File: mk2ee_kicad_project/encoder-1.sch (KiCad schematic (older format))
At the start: 15 parts, among them J6 Conn_01x05_Male, J7 Conn_01x05_Male, J8 Conn_01x02_Male, U7 74HC595, U8 AS5047D-ATSM

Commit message: all components are checked
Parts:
- removed J6, J7: Conn_01x05_Male, Connector_Molex:Molex_CLIK-Mate_502443-0570_1x05-1MP_P2.00mm_Vertical, symbol Connector:Conn_01x05_Male
- removed J8: Conn_01x02_Male, Connector_Molex:Molex_CLIK-Mate_502443-0270_1x02-1MP_P2.00mm_Vertical, symbol Connector:Conn_01x02_Male
- added J10: Conn_01x02_Male, MK2Library:Molex_MicroClasp_55932-0210_1x02_P2.00mm_Vertical, symbol Connector:Conn_01x02_Male
- added J8, J9: Conn_02x03_Male, Connector_IDC:IDC-Header_2x03_P2.54mm_Horizontal, symbol Connector:Conn_01x06_Male
- R10, R13: value 45 -> 100; footprint Resistor_SMD:R_0805_2012Metric_Pad1.15x1.40mm_HandSolder -> Resistor_SMD:R_1206_3216Metric; Manufacturer (none) -> MULTICOMP PRO; Name (none) -> MCWR12X1000FTL
- R11, R14: value 86.6 -> 270; footprint Resistor_SMD:R_0805_2012Metric_Pad1.15x1.40mm_HandSolder -> Resistor_SMD:R_1206_3216Metric; Manufacturer (none) -> MULTICOMP PRO; Name (none) -> MCWR12X2700FTL
- R12, R9: value 24 -> 82; footprint Resistor_SMD:R_0805_2012Metric_Pad1.15x1.40mm_HandSolder -> Resistor_SMD:R_1206_3216Metric; Manufacturer (none) -> MULTICOMP PRO; Name (none) -> MCWR12X82R0FTL
- U9: renamed from U7; footprint (none) -> MK2Library:SN74HC595PWR; Manufacturer (none) -> Texas Instruments; Name (none) -> SN74HC595PWR
- renumbered C18 to C20, C19 to C21
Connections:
- net VCC3 is gone; now on net VCCD3v3: C21.1, U8.11 (VDD), U8.12 (VDD3V)
- net CLKEn3: now also J8.3 (Pin_3), J9.3 (Pin_3)
- net GND: now also J10.1 (Pin_1)
- net MISO3: now also J8.4 (Pin_4), J9.4 (Pin_4)
- net PO-CLKEn3: now also J8.1 (Pin_1), J9.1 (Pin_1)
- net SH-CLKEn3: now also J8.5 (Pin_5), J9.5 (Pin_5)
- net SerialDataInEn3: now also J8.2 (Pin_2)
- net SerialDataOutEn3: now also J9.2 (Pin_2)
- net VCCD3v3: now also J10.2 (Pin_2)
- no-connect marks 8 -> 10

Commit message: PCB design is updated
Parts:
- removed C21: 100nF, Capacitor_SMD:CP_Elec_6.3x7.7, symbol Device:CP1
- added C21: 100nF, Capacitor_SMD:C_1206_3216Metric, symbol Device:C
- C20: footprint (none) -> Capacitor_SMD:C_1206_3216Metric; Manufacturer (none) -> Kemet; Name (none) -> C1206C104K5RACTU
- R10, R13: value 100 -> 100R
- R11, R14: value 270 -> 270R
- R12, R9: value 82 -> 82R
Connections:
- net GND: now also C21.2
- net VCCD3v3: now also C21.1
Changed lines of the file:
@@
-$EndComp
-$Comp
-L Device:CP1 C?
-U 1 1 5F504AEC
-P 7400 2600
-AR Path="/5F455032/5F504AEC" Ref="C?"  Part="1"
-AR Path="/5F4C6BF4/5F504AEC" Ref="C?"  Part="1"
-AR Path="/5F4C6CE4/5F504AEC" Ref="C21"  Part="1"
-F 0 "C21" H 7515 2646 50  0000 L CNN
-F 1 "100nF" H 7515 2555 50  0000 L CNN
-F 2 "Capacitor_SMD:CP_Elec_6.3x7.7" H 7400 2600 50  0001 C CNN
-F 3 "~" H 7400 2600 50  0001 C CNN
-F 4 "EDK106M063A9GAA" H 7400 2600 50  0001 C CNN "Name"
-F 5 "Kemet" H 7400 2600 50  0001 C CNN "Manufacturer"
-	1    7400 2600
-	1    0    0    -1
 $EndComp
 $Comp
@@
 AR Path="/5F4C6CE4/5F504B1E" Ref="R11"  Part="1"
 F 0 "R11" H 4580 4304 50  0000 R CNN
-F 1 "270" H 4580 4395 50  0000 R CNN
+F 1 "270R" H 4580 4395 50  0000 R CNN
 F 2 "Resistor_SMD:R_1206_3216Metric" V 4580 4350 50  0001 C CNN
 F 3 "~" H 4650 4350 50  0001 C CNN
@@
 AR Path="/5F4C6CE4/5F504B30" Ref="R10"  Part="1"
 F 0 "R10" H 2080 4404 50  0000 R CNN
-F 1 "100" H 2080 4495 50  0000 R CNN
+F 1 "100R" H 2080 4495 50  0000 R CNN
 F 2 "Resistor_SMD:R_1206_3216Metric" V 2080 4450 50  0001 C CNN
 F 3 "~" H 2150 4450 50  0001 C CNN
@@
 AR Path="/5F4C6CE4/5F504B49" Ref="R9"  Part="1"
 F 0 "R9" H 1680 4304 50  0000 R CNN
-F 1 "82" H 1680 4395 50  0000 R CNN
+F 1 "82R" H 1680 4395 50  0000 R CNN
 F 2 "Resistor_SMD:R_1206_3216Metric" V 1680 4350 50  0001 C CNN
 F 3 "~" H 1750 4350 50  0001 C CNN
@@
 Wire Wire Line
 	2750 2200 2750 1300
-Connection ~ 2750 1300
 Wire Wire Line
 	2750 1300 3300 1300
-Wire Wire Line
-	2250 1300 2450 1300
-$Comp
-L Device:C C20
-U 1 1 5F941CAA
-P 2450 1450
-F 0 "C20" H 2565 1496 50  0000 L CNN
-F 1 "100nF" H 2565 1405 50  0000 L CNN
-F 2 "" H 2488 1300 50  0001 C CNN
-F 3 "~" H 2450 1450 50  0001 C CNN
-	1    2450 1450
-	1    0    0    -1
-$EndComp
-Connection ~ 2450 1300
-Wire Wire Line
-	2450 1300 2750 1300
 $Comp
 L power:GND #PWR0148
@@
 AR Path="/5F4C6CE4/6022AF4A" Ref="R12"  Part="1"
 F 0 "R12" H 1680 5604 50  0000 R CNN
-F 1 "82" H 1680 5695 50  0000 R CNN
+F 1 "82R" H 1680 5695 50  0000 R CNN
 F 2 "Resistor_SMD:R_1206_3216Metric" V 1680 5650 50  0001 C CNN
 F 3 "~" H 1750 5650 50  0001 C CNN
@@
 AR Path="/5F4C6CE4/6022B39A" Ref="R13"  Part="1"
 F 0 "R13" H 2080 5704 50  0000 R CNN
-F 1 "100" H 2080 5795 50  0000 R CNN
+F 1 "100R" H 2080 5795 50  0000 R CNN
 F 2 "Resistor_SMD:R_1206_3216Metric" V 2080 5750 50  0001 C CNN
 F 3 "~" H 2150 5750 50  0001 C CNN
@@
 AR Path="/5F4C6CE4/6022C64F" Ref="R14"  Part="1"
 F 0 "R14" H 4580 5604 50  0000 R CNN
-F 1 "270" H 4580 5695 50  0000 R CNN
+F 1 "270R" H 4580 5695 50  0000 R CNN
 F 2 "Resistor_SMD:R_1206_3216Metric" V 4580 5650 50  0001 C CNN
 F 3 "~" H 4650 5650 50  0001 C CNN
@@
 Text Label 3150 1300 2    50   ~ 0
 pwr11
+$Comp
+L Device:C C21
+U 1 1 6032EA5A
+P 7400 2600
+AR Path="/5F4C6CE4/6032EA5A" Ref="C21"  Part="1"
+AR Path="/5F475AB3/6032EA5A" Ref="C?"  Part="1"
+F 0 "C21" H 7515 2646 50  0000 L CNN
+F 1 "100nF" H 7515 2555 50  0000 L CNN
+F 2 "Capacitor_SMD:C_1206_3216Metric" H 7438 2450 50  0001 C CNN
+F 3 "~" H 7400 2600 50  0001 C CNN
+F 4 "C1206C104K5RACTU" H 7400 2600 50  0001 C CNN "Name"
+F 5 "Kemet" H 7400 2600 50  0001 C CNN "Manufacturer"
+	1    7400 2600
+	1    0    0    -1
+$EndComp
+$Comp
+L Device:C C20
+U 1 1 603306B0
+P 2450 1450
+AR Path="/5F4C6CE4/603306B0" Ref="C20"  Part="1"
+AR Path="/5F475AB3/603306B0" Ref="C?"  Part="1"
+F 0 "C20" H 2565 1496 50  0000 L CNN
+F 1 "100nF" H 2565 1405 50  0000 L CNN
+F 2 "Capacitor_SMD:C_1206_3216Metric" H 2488 1300 50  0001 C CNN
+F 3 "~" H 2450 1450 50  0001 C CNN
+F 4 "C1206C104K5RACTU" H 2450 1450 50  0001 C CNN "Name"
+F 5 "Kemet" H 2450 1450 50  0001 C CNN "Manufacturer"
+	1    2450 1450
+	1    0    0    -1
+$EndComp
+Wire Wire Line
+	2250 1300 2450 1300
+Connection ~ 2750 1300
+Connection ~ 2450 1300
+Wire Wire Line
+	2450 1300 2750 1300
 $EndSCHEMATC

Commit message: all components are connected
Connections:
- net CLKEn3: now also J8.4 (Pin_4), J9.4 (Pin_4); no longer J8.3 (Pin_3), J9.3 (Pin_3)
- net CSn3: now also U9.7 (QH); no longer U9.15 (QA)
- net LED2-B3: now also U9.4 (QE); no longer U9.6 (QG)
- net LED2-R3: now also U9.6 (QG); no longer U9.4 (QE)
- net MISO3: now also J8.6 (Pin_6), J9.2 (Pin_2); no longer J8.4 (Pin_4), J9.4 (Pin_4)
- net PO-CLKEn3: now also J8.3 (Pin_3), J9.3 (Pin_3); no longer J8.1 (Pin_1), J9.1 (Pin_1)
- net SH-CLKEn3: now also J9.1 (Pin_1); no longer J9.5 (Pin_5)
- net SerialDataInEn3: now also J8.1 (Pin_1); no longer J8.2 (Pin_2)
- net SerialDataOutEn3: now also J9.5 (Pin_5); no longer J9.2 (Pin_2)
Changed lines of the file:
@@
 Comment4 ""
 $EndDescr
-Text GLabel 3950 1900 2    50   Output ~ 0
+Text GLabel 3950 2600 2    50   Output ~ 0
 CSn3
 Text GLabel 3950 2000 2    50   Output ~ 0
@@
 Text GLabel 3950 2200 2    50   Output ~ 0
 LED1-B3
-Text GLabel 3950 2300 2    50   Output ~ 0
+Text GLabel 3950 2500 2    50   Output ~ 0
 LED2-R3
 Text GLabel 3950 2400 2    50   Output ~ 0
 LED2-G3
-NoConn ~ 3700 2600
-Wire Wire Line
-	3700 1900 3950 1900
+Wire Wire Line
+	3700 2600 3950 2600
 Wire Wire Line
 	3700 2000 3950 2000
@@
 	3700 2200 3950 2200
 Wire Wire Line
-	3700 2300 3950 2300
+	3700 2500 3950 2500
 Wire Wire Line
 	3700 2400 3950 2400
-Text GLabel 9150 2000 0    50   Output ~ 0
+Text GLabel 9150 1900 0    50   Output ~ 0
 CLKEn3
-Text GLabel 9150 1900 0    50   Input ~ 0
+Text GLabel 9150 1700 0    50   Input ~ 0
 MISO3
 Text GLabel 9150 1800 0    50   Output ~ 0
 SH-CLKEn3
-Text GLabel 9150 2100 0    50   Output ~ 0
+Text GLabel 9150 2200 0    50   Output ~ 0
 SerialDataInEn3
-Text GLabel 9150 2200 0    50   Output ~ 0
+Text GLabel 9150 2000 0    50   Output ~ 0
 PO-CLKEn3
 Wire Wire Line
 	9150 1800 9400 1800
 Wire Wire Line
+	9150 1700 9400 1700
+Wire Wire Line
 	9150 1900 9400 1900
 Wire Wire Line
+	9150 2200 9400 2200
+Wire Wire Line
 	9150 2000 9400 2000
 Wire Wire Line
-	9150 2100 9400 2100
-Wire Wire Line
-	9150 2200 9400 2200
+	9150 3050 9400 3050
+Wire Wire Line
+	9150 2950 9400 2950
+Wire Wire Line
+	9150 2750 9400 2750
 Wire Wire Line
 	9150 2650 9400 2650
 Wire Wire Line
-	9150 2750 9400 2750
-Wire Wire Line
 	9150 2850 9400 2850
-Wire Wire Line
-	9150 2950 9400 2950
-Wire Wire Line
-	9150 3050 9400 3050
 Text GLabel 2250 1300 0    50   Input ~ 0
 VCCD3v3
@@
 Wire Wire Line
 	2650 1900 2900 1900
-Text GLabel 3950 2500 2    50   Output ~ 0
+Text GLabel 3950 2300 2    50   Output ~ 0
 LED2-B3
 Wire Wire Line
-	3700 2500 3950 2500
+	3700 2300 3950 2300
+Text GLabel 9150 2750 0    50   Input ~ 0
+CLKEn3
+Text GLabel 9150 2950 0    50   Output ~ 0
+MISO3
+Text GLabel 9150 3050 0    50   Input ~ 0
+SH-CLKEn3
+Text GLabel 9150 2650 0    50   Input ~ 0
+SerialDataOutEn3
 Text GLabel 9150 2850 0    50   Input ~ 0
-CLKEn3
-Text GLabel 9150 2750 0    50   Output ~ 0
-MISO3
-Text GLabel 9150 2650 0    50   Input ~ 0
-SH-CLKEn3
-Text GLabel 9150 2950 0    50   Input ~ 0
-SerialDataOutEn3
-Text GLabel 9150 3050 0    50   Input ~ 0
 PO-CLKEn3
 $Comp
@@
 	-1   0    0    1
 $EndComp
-NoConn ~ 9400 2550
-NoConn ~ 9400 1700
 $Comp
 L Connector:Conn_01x02_Male J?
@@
 Wire Wire Line
 	2450 1300 2750 1300
+NoConn ~ 3700 1900
+NoConn ~ 9400 2100
+NoConn ~ 9400 2550
 $EndSCHEMATC

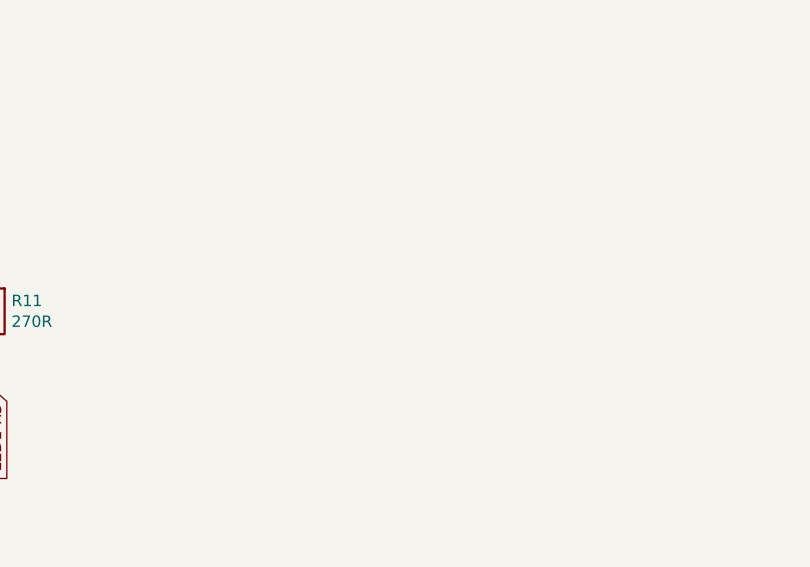
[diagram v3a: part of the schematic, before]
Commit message: New 3D model of Base part and PCB design is fixed
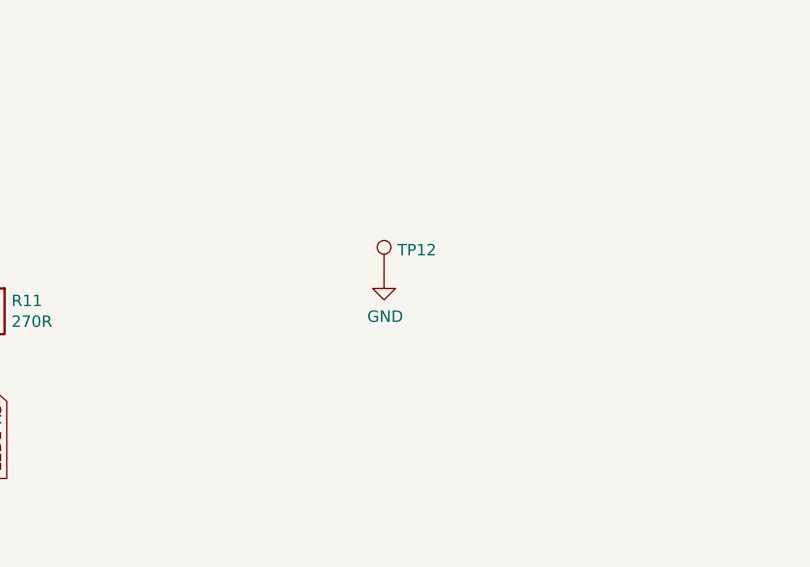
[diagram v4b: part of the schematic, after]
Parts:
- added TP12: TestPoint, TestPoint:TestPoint_THTPad_D1.0mm_Drill0.5mm, symbol Connector:TestPoint
- C20, C21: footprint Capacitor_SMD:C_1206_3216Metric -> Capacitor_SMD:C_1206_3216Metric_Pad1.42x1.75mm_HandSolder
- R10, R11, R12, R13, R14, R9: footprint Resistor_SMD:R_1206_3216Metric -> Resistor_SMD:R_1206_3216Metric_Pad1.42x1.75mm_HandSolder
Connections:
- net GND: now also TP12.1
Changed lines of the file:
@@
 F 0 "R11" H 4580 4304 50  0000 R CNN
 F 1 "270R" H 4580 4395 50  0000 R CNN
-F 2 "Resistor_SMD:R_1206_3216Metric" V 4580 4350 50  0001 C CNN
+F 2 "Resistor_SMD:R_1206_3216Metric_Pad1.42x1.75mm_HandSolder" V 4580 4350 50  0001 C CNN
 F 3 "~" H 4650 4350 50  0001 C CNN
 F 4 "MCWR12X2700FTL" H 4650 4350 50  0001 C CNN "Name"
@@
 F 0 "R10" H 2080 4404 50  0000 R CNN
 F 1 "100R" H 2080 4495 50  0000 R CNN
-F 2 "Resistor_SMD:R_1206_3216Metric" V 2080 4450 50  0001 C CNN
+F 2 "Resistor_SMD:R_1206_3216Metric_Pad1.42x1.75mm_HandSolder" V 2080 4450 50  0001 C CNN
 F 3 "~" H 2150 4450 50  0001 C CNN
 F 4 "MCWR12X1000FTL" H 2150 4450 50  0001 C CNN "Name"
@@
 F 0 "R9" H 1680 4304 50  0000 R CNN
 F 1 "82R" H 1680 4395 50  0000 R CNN
-F 2 "Resistor_SMD:R_1206_3216Metric" V 1680 4350 50  0001 C CNN
+F 2 "Resistor_SMD:R_1206_3216Metric_Pad1.42x1.75mm_HandSolder" V 1680 4350 50  0001 C CNN
 F 3 "~" H 1750 4350 50  0001 C CNN
 F 4 "MCWR12X82R0FTL" H 1750 4350 50  0001 C CNN "Name"
@@
 F 0 "R12" H 1680 5604 50  0000 R CNN
 F 1 "82R" H 1680 5695 50  0000 R CNN
-F 2 "Resistor_SMD:R_1206_3216Metric" V 1680 5650 50  0001 C CNN
+F 2 "Resistor_SMD:R_1206_3216Metric_Pad1.42x1.75mm_HandSolder" V 1680 5650 50  0001 C CNN
 F 3 "~" H 1750 5650 50  0001 C CNN
 F 4 "MCWR12X82R0FTL" H 1750 5650 50  0001 C CNN "Name"
@@
 F 0 "R13" H 2080 5704 50  0000 R CNN
 F 1 "100R" H 2080 5795 50  0000 R CNN
-F 2 "Resistor_SMD:R_1206_3216Metric" V 2080 5750 50  0001 C CNN
+F 2 "Resistor_SMD:R_1206_3216Metric_Pad1.42x1.75mm_HandSolder" V 2080 5750 50  0001 C CNN
 F 3 "~" H 2150 5750 50  0001 C CNN
 F 4 "MCWR12X1000FTL" H 2150 5750 50  0001 C CNN "Name"
@@
 F 0 "R14" H 4580 5604 50  0000 R CNN
 F 1 "270R" H 4580 5695 50  0000 R CNN
-F 2 "Resistor_SMD:R_1206_3216Metric" V 4580 5650 50  0001 C CNN
+F 2 "Resistor_SMD:R_1206_3216Metric_Pad1.42x1.75mm_HandSolder" V 4580 5650 50  0001 C CNN
 F 3 "~" H 4650 5650 50  0001 C CNN
 F 4 "MCWR12X2700FTL" H 4650 5650 50  0001 C CNN "Name"
@@
 F 0 "C21" H 7515 2646 50  0000 L CNN
 F 1 "100nF" H 7515 2555 50  0000 L CNN
-F 2 "Capacitor_SMD:C_1206_3216Metric" H 7438 2450 50  0001 C CNN
+F 2 "Capacitor_SMD:C_1206_3216Metric_Pad1.42x1.75mm_HandSolder" H 7438 2450 50  0001 C CNN
 F 3 "~" H 7400 2600 50  0001 C CNN
 F 4 "C1206C104K5RACTU" H 7400 2600 50  0001 C CNN "Name"
@@
 F 0 "C20" H 2565 1496 50  0000 L CNN
 F 1 "100nF" H 2565 1405 50  0000 L CNN
-F 2 "Capacitor_SMD:C_1206_3216Metric" H 2488 1300 50  0001 C CNN
+F 2 "Capacitor_SMD:C_1206_3216Metric_Pad1.42x1.75mm_HandSolder" H 2488 1300 50  0001 C CNN
 F 3 "~" H 2450 1450 50  0001 C CNN
 F 4 "C1206C104K5RACTU" H 2450 1450 50  0001 C CNN "Name"
@@
 NoConn ~ 9400 2100
 NoConn ~ 9400 2550
+$Comp
+L Connector:TestPoint TP?
+U 1 1 608DB947
+P 6350 4200
+AR Path="/5F455032/608DB947" Ref="TP?"  Part="1"
+AR Path="/5F4C637B/608DB947" Ref="TP?"  Part="1"
+AR Path="/5F475AB3/608DB947" Ref="TP?"  Part="1"
+AR Path="/5F4C6CE4/608DB947" Ref="TP12"  Part="1"
+F 0 "TP12" H 6408 4318 50  0000 L CNN
+F 1 "TestPoint" H 6408 4227 50  0001 L CNN
+F 2 "TestPoint:TestPoint_THTPad_D1.0mm_Drill0.5mm" H 6550 4200 50  0001 C CNN
+F 3 "~" H 6550 4200 50  0001 C CNN
+	1    6350 4200
+	1    0    0    -1
+$EndComp
+$Comp
+L power:GND #PWR?
+U 1 1 608DD01D
+P 6350 4200
+AR Path="/5F4C6CE4/608DD01D" Ref="#PWR?"  Part="1"
+AR Path="/5F4C6BF4/608DD01D" Ref="#PWR?"  Part="1"
+F 0 "#PWR?" H 6350 3950 50  0001 C CNN
+F 1 "GND" H 6355 4027 50  0000 C CNN
+F 2 "" H 6350 4200 50  0001 C CNN
+F 3 "" H 6350 4200 50  0001 C CNN
+	1    6350 4200
+	1    0    0    -1
+$EndComp
 $EndSCHEMATC
